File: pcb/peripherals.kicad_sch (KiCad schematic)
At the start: 5 parts, among them J10 SPI, J14 SERIAL, J3 INDICATOR, J8 QWIIC1, J9 QWIIC2

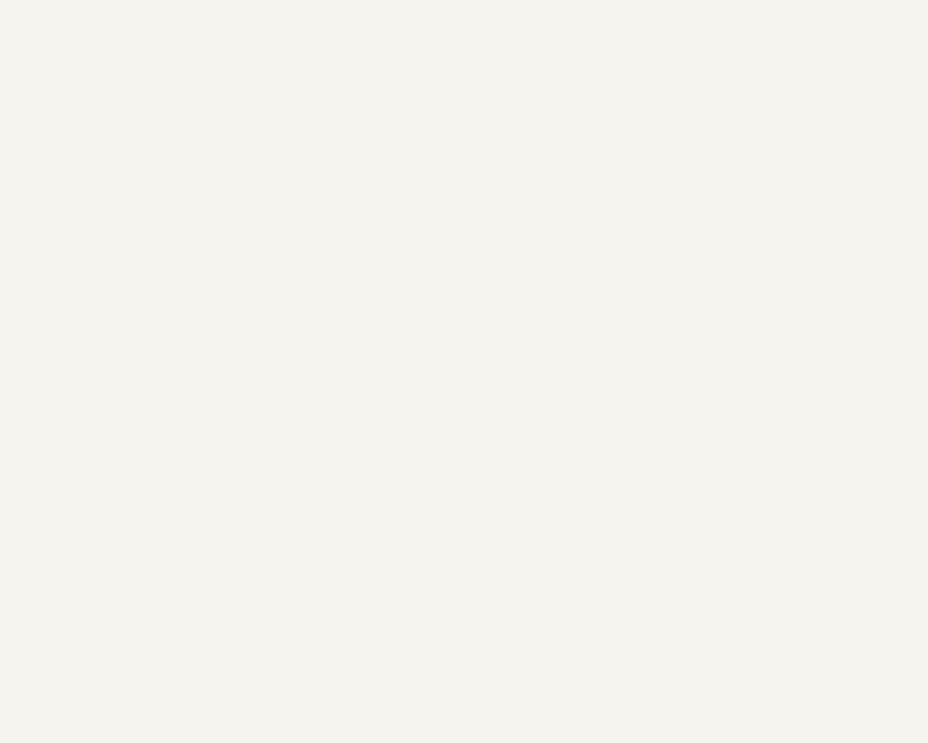
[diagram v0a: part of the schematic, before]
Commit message: Added buzzer
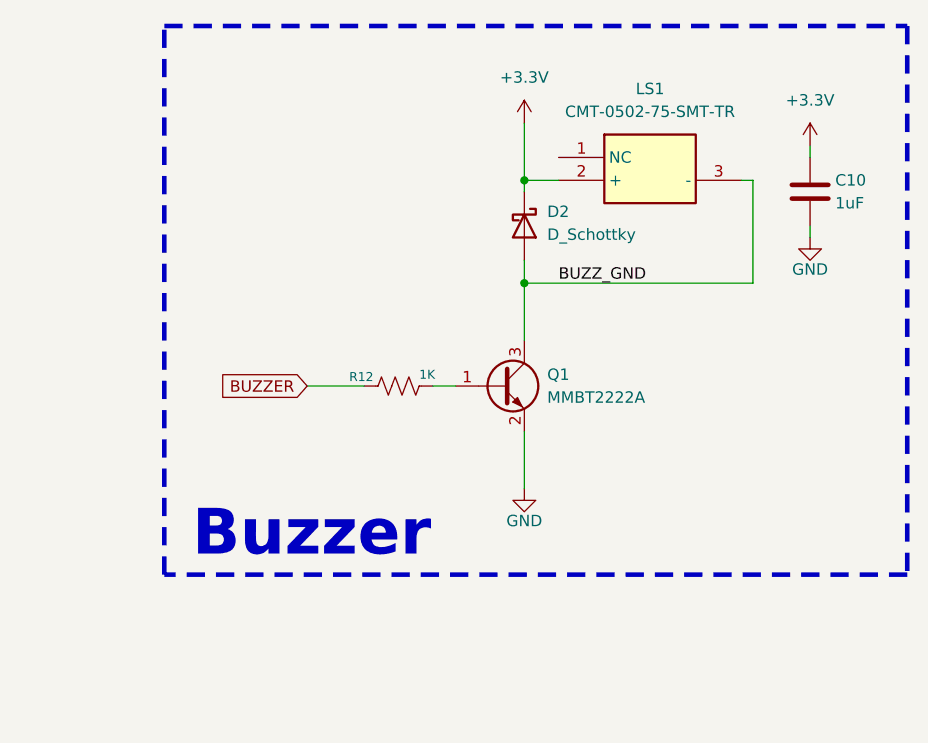
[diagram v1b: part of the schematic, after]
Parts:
- added C10: 1uF, Capacitor_SMD:C_0603_1608Metric, symbol Device:C
- added D2: D_Schottky, Diode_SMD:D_SOD-523, symbol Device:D_Schottky
- added LS1: CMT-0502-75-SMT-TR, CRG Makes:CMT050275SMTTR, symbol CRG Makes:CMT-0502-75-SMT-TR
- added Q1: MMBT2222A, Package_TO_SOT_SMD:SOT-523, symbol Transistor_BJT:MMBT2222A
- added R12: 1K, Resistor_SMD:R_0603_1608Metric, symbol Device:R_US
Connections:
- net +3.3V: now also C10.1, D2.1 (K), LS1.2 (+)
- net GND: now also C10.2, Q1.2 (E)
- new net: Q1.1 (B), R12.2
- new net BUZZER: R12.1
- new net BUZZ_GND: D2.2 (A), LS1.3 (-), Q1.3 (C)
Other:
- note added: "Buzzer"

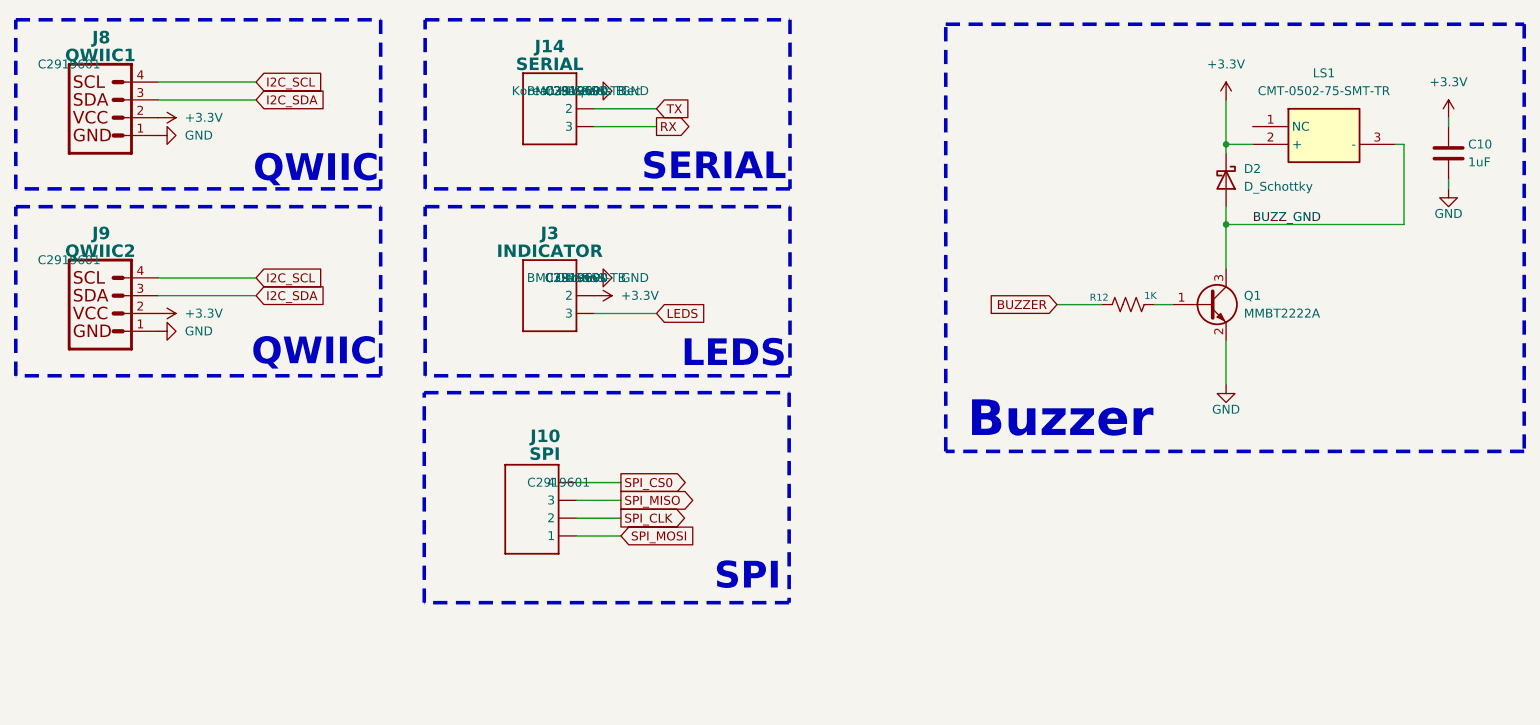
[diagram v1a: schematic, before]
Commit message: Changed SPI to 8 pin connector
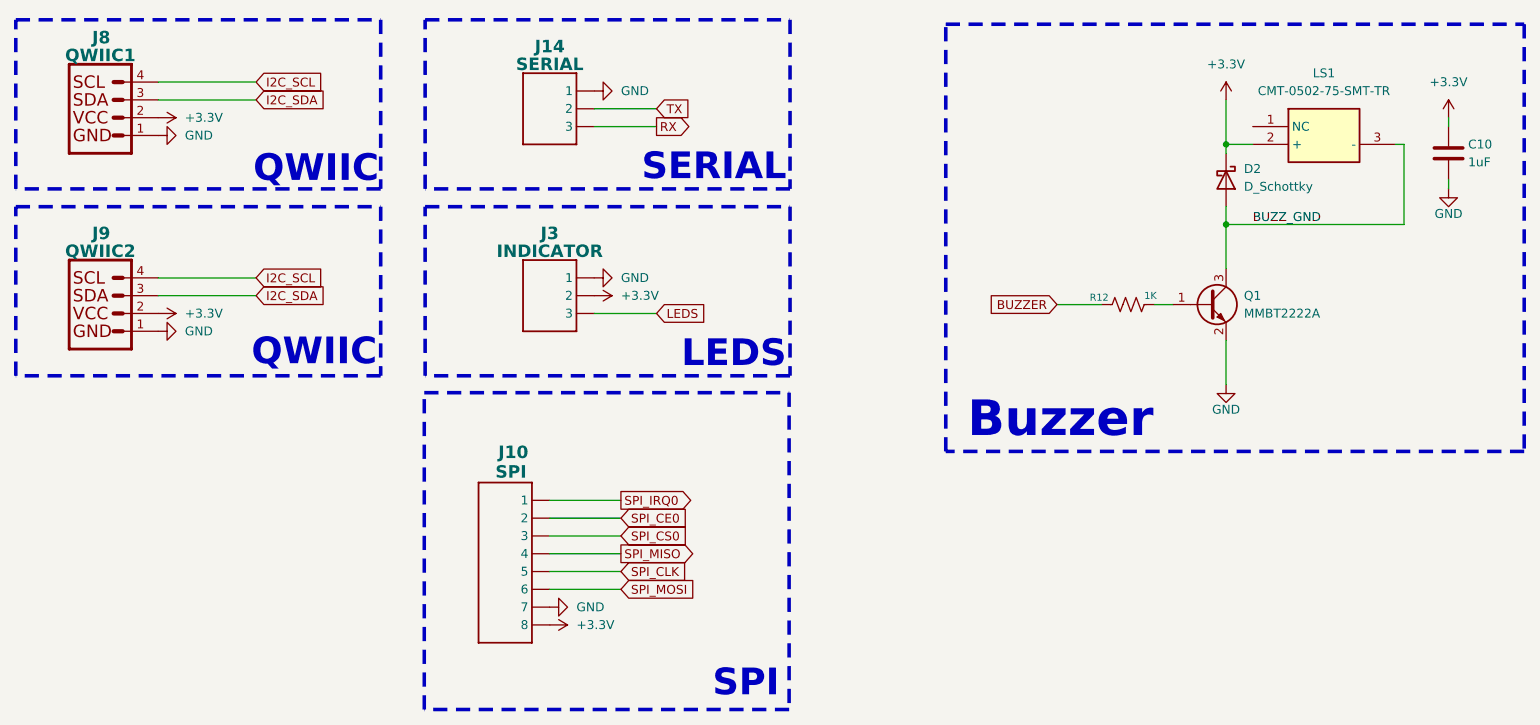
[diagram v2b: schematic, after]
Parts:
- J10: footprint CRGM Connector:JST_SH_BM04B-SRSS-TB_1x04-1MP_P1.00mm_Vertical -> Connector_JST:JST_SH_BM08B-SRSS-TB_1x08-1MP_P1.00mm_Vertical; symbol CRGM Connector:JST-SH-4 -> CRGM Connector:JST-SH-8
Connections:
- net +3.3V: now also J10.8
- net GND: now also J10.7
- net SPI_CLK: now also J10.5; no longer J10.2
- net SPI_CS0: now also J10.3; no longer J10.4
- net SPI_MISO: now also J10.4; no longer J10.3
- net SPI_MOSI: now also J10.6; no longer J10.1
- new net SPI_CE0: J10.2
- new net SPI_IRQ0: J10.1

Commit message: Added additional labels; minor clean up.
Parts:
- J10: Digikey (none) -> 455-BM08B-SRSS-TBTR-ND; LCSC C2919601 -> C2845376; MPN BM04B-SRSS-TB -> BM08B-SRSS-TB(LF)(SN); Mouser (none) -> 306-BM08BSRSSTBLFSN
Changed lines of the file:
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@@
 			)
 		)
-		(property "Description" "JST SH 1.0mm 6 Position"
+		(property "Description" "8 position, 1mm connector"
 			(at 107.95 81.28 0)
 			(effects
@@
 			)
 		)
-		(property "MPN" "BM04B-SRSS-TB"
+		(property "MPN" "BM08B-SRSS-TB(LF)(SN)"
 			(at 107.95 81.28 0)
 			(effects
@@
 			)
 		)
-		(property "LCSC" "C2919601"
+		(property "LCSC" "C2845376"
 			(at 107.95 81.28 0)
 			(effects
@@
 			)
 		)
-		(property "Mouser" ""
+		(property "Mouser" "306-BM08BSRSSTBLFSN"
 			(at 107.95 81.28 0)
 			(effects
@@
 			)
 		)
-		(property "Digikey" ""
+		(property "Digikey" "455-BM08B-SRSS-TBTR-ND"
 			(at 107.95 81.28 0)
 			(effects

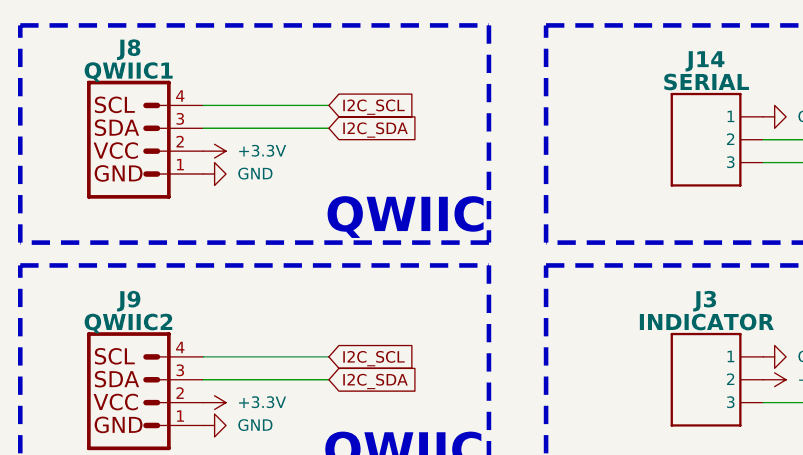
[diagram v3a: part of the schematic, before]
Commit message: Change panel to be 1x1
Changed connectors be vertical rather than horizontal.
Updated TVS diodes to DFN1006 rather than SMF
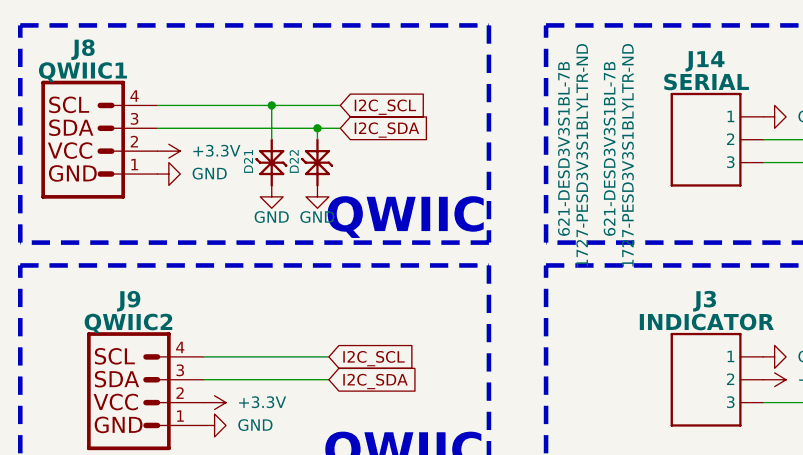
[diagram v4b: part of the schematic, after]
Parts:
- added D21, D22: PESD3V3S1BL, CRGM Passive:DFN1006-2, symbol CRGM Passive:PESD3V3S1BL
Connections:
- net GND: now also D21.1 (K1), D22.1 (K1)
- net I2C_SCL: now also D21.2 (K2)
- net I2C_SDA: now also D22.2 (K2)
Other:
- moved on the sheet: J8

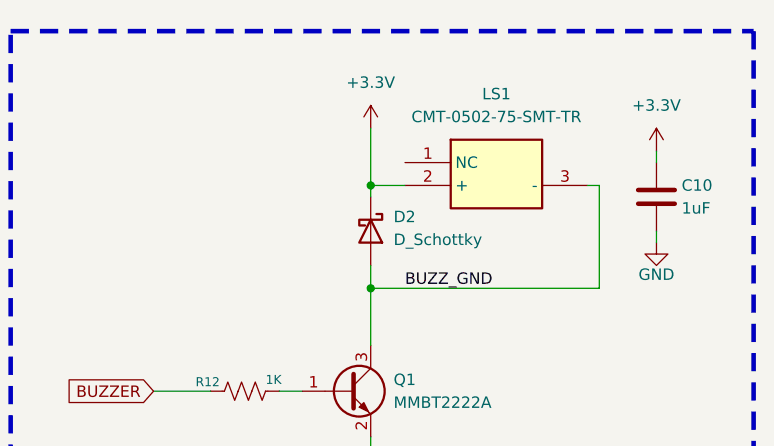
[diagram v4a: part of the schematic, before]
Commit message: Major overhaul of IO
Added GPIO module
Added SPI interface
Added serial interface
Added power selection
Added power LEDs
Changed v3.3 LDO
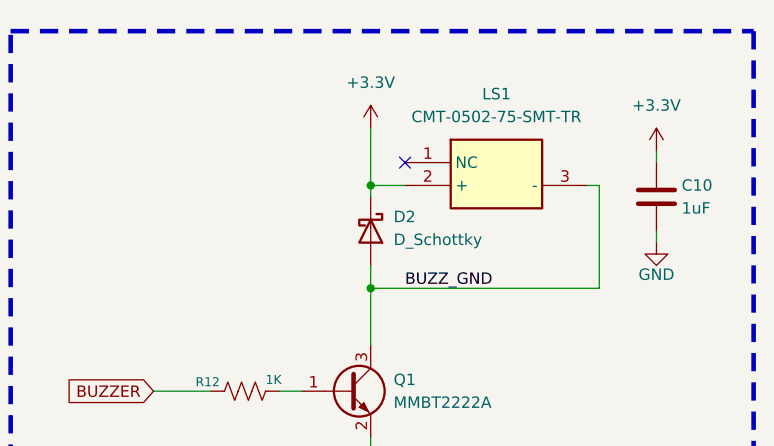
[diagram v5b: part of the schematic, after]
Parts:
- J10: footprint Connector_JST:JST_SH_BM08B-SRSS-TB_1x08-1MP_P1.00mm_Vertical -> CRGM Connector:JST_SH_BM08B-SRSS-TB_1x08-1MP_P1.00mm_Vertical
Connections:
- no-connect marks 0 -> 1

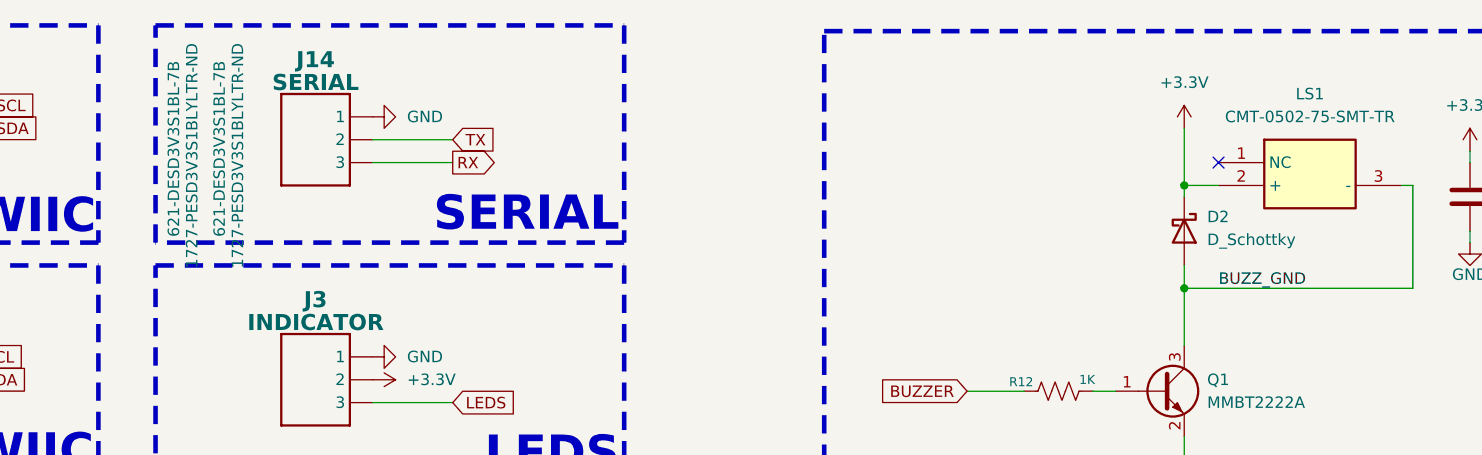
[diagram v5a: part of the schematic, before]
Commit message: Fixed MPN mismatches and other fields
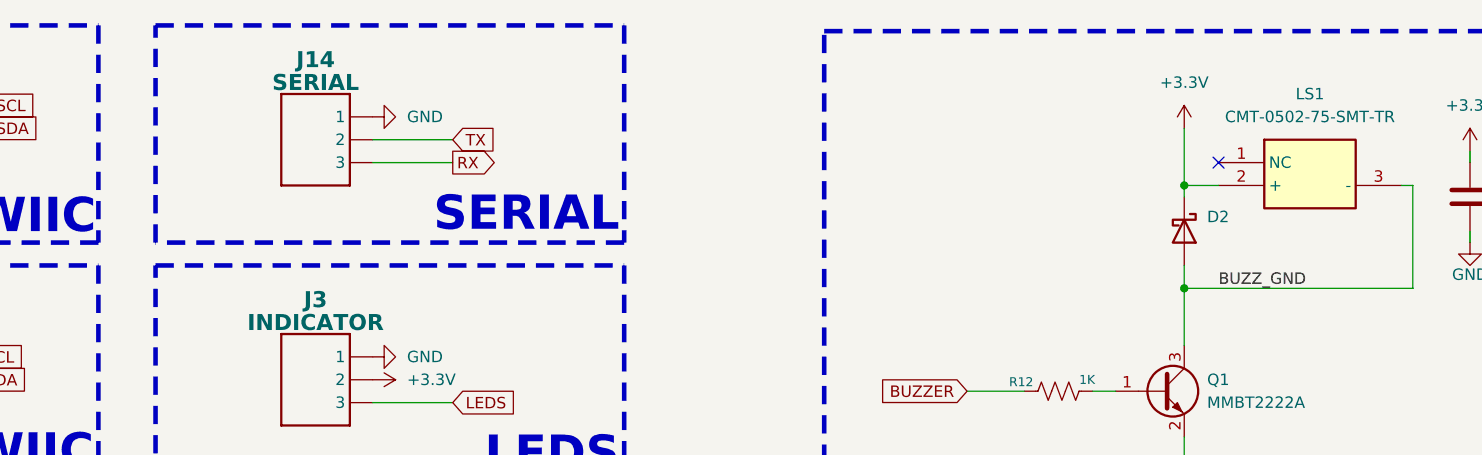
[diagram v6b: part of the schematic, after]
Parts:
- J14: footprint CRGM Connector:JST_SH_BM03B-SRSS-TB_1x03-1MP_P1.00mm_Vertical -> Connector_JST:JST_SH_BM03B-SRSS-TB_1x03-1MP_P1.00mm_Vertical; MN Korean Hroparts Elec -> JST
- J3: MN Omron -> JST
- LS1: MF (none) -> Same Sky
- Q1: MF (none) -> Diodes Incorporated
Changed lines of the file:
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@@
 					(size 1.27 1.27)
 				)
+				(hide yes)
 			)
 		)
@@
 					(size 1.27 1.27)
 				)
+				(hide yes)
 			)
 		)
@@
 					(size 1.27 1.27)
 				)
+				(hide yes)
 			)
 		)
@@
 					(size 1.27 1.27)
 				)
+				(hide yes)
+			)
+		)
+		(property "Digikey" ""
+			(at 193.04 55.88 0)
+			(effects
+				(font
+					(size 1.27 1.27)
+				)
+				(hide yes)
+			)
+		)
+		(property "Mouser" ""
+			(at 193.04 55.88 0)
+			(effects
+				(font
+					(size 1.27 1.27)
+				)
+				(hide yes)
 			)
 		)
@@
 				)
 				(justify left)
+				(hide yes)
 			)
 		)
@@
 					(size 1.27 1.27)
 				)
+				(hide yes)
 			)
 		)
@@
 					(size 1.27 1.27)
 				)
+				(hide yes)
 			)
 		)
@@
 					(size 1.27 1.27)
 				)
+				(hide yes)
 			)
 		)
@@
 					(size 1.27 1.27)
 				)
+				(hide yes)
+			)
+		)
+		(property "Digikey" ""
+			(at 207.01 38.1 0)
+			(effects
+				(font
+					(size 1.27 1.27)
+				)
+				(hide yes)
+			)
+		)
+		(property "Mouser" ""
+			(at 207.01 38.1 0)
+			(effects
+				(font
+					(size 1.27 1.27)
+				)
+				(hide yes)
 			)
 		)
@@
 					(size 1.27 1.27)
 				)
+				(hide yes)
 			)
 		)
@@
 					(size 1.27 1.27)
 				)
+				(hide yes)
 			)
 		)
@@
 					(size 1.27 1.27)
 				)
+				(hide yes)
 			)
 		)
@@
 					(size 1.27 1.27)
 				)
+				(hide yes)
 			)
 		)
@@
 					(size 1.27 1.27)
 				)
+				(hide yes)
 			)
 		)
@@
 					(size 1.27 1.27)
 				)
+				(hide yes)
 			)
 		)
@@
 					(size 1.27 1.27)
 				)
+				(hide yes)
 			)
 		)
@@
 					(size 1.27 1.27)
 				)
+				(hide yes)
 			)
 		)
@@
 					(size 1.27 1.27)
 				)
+				(hide yes)
 			)
 		)
@@
 					(size 1.27 1.27)
 				)
+				(hide yes)
+			)
+		)
+		(property "MF" "Diodes Incorporated"
+			(at 204.47 55.88 0)
+			(effects
+				(font
+					(size 1.27 1.27)
+				)
+				(hide yes)
 			)
 		)
@@
 					(size 1.27 1.27)
 				)
+				(hide yes)
 			)
 		)
@@
 					(size 1.27 1.27)
 				)
+				(hide yes)
 			)
 		)
@@
 					(size 1.27 1.27)
 				)
+				(hide yes)
 			)
 		)
@@
 					(size 1.27 1.27)
 				)
+				(hide yes)
 			)
 		)
@@
 			)
 		)
-		(property "Footprint" "CRGM Connector:JST_SH_BM03B-SRSS-TB_1x03-1MP_P1.00mm_Vertical"
+		(property "Footprint" "Connector_JST:JST_SH_BM03B-SRSS-TB_1x03-1MP_P1.00mm_Vertical"
 			(at 113.03 16.51 0)
 			(effects
@@
 			)
 		)
-		(property "MN" "Korean Hroparts Elec"
+		(property "MN" "JST"
 			(at 114.3 25.4 0)
 			(effects
@@
 					(size 1.27 1.27)
 				)
+				(hide yes)
 			)
 		)
@@
 					(size 1.27 1.27)
 				)
+				(hide yes)
 			)
 		)
@@
 					(size 1.27 1.27)
 				)
+				(hide yes)
 			)
 		)
@@
 					(size 1.27 1.27)
 				)
+				(hide yes)
+			)
+		)
+		(property "Digikey" ""
+			(at 114.3 25.4 0)
+			(effects
+				(font
+					(size 1.27 1.27)
+				)
+				(hide yes)
+			)
+		)
+		(property "Mouser" ""
+			(at 114.3 25.4 0)
+			(effects
+				(font
+					(size 1.27 1.27)
+				)
+				(hide yes)
 			)
 		)
@@
 					(size 1.27 1.27)
 				)
+				(hide yes)
 			)
 		)
@@
 					(size 1.27 1.27)
 				)
+				(hide yes)
 			)
 		)
@@
 					(size 1.27 1.27)
 				)
+				(hide yes)
 			)
 		)
@@
 					(size 1.27 1.27)
 				)
+				(hide yes)
+			)
+		)
+		(property "Digikey" ""
+			(at 238.76 34.29 0)
+			(effects
+				(font
+					(size 1.27 1.27)
+				)
+				(hide yes)
+			)
+		)
+		(property "Mouser" ""
+			(at 238.76 34.29 0)
+			(effects
+				(font
+					(size 1.27 1.27)
+				)
+				(hide yes)
 			)
 		)
@@
 					(size 1.27 1.27)
 				)
+				(hide yes)
 			)
 		)
@@
 					(size 1.27 1.27)
 				)
+				(hide yes)
 			)
 		)
@@
 					(size 1.27 1.27)
 				)
+				(hide yes)
 			)
 		)
@@
 					(size 1.27 1.27)
 				)
+				(hide yes)
 			)
 		)
@@
 					(size 1.27 1.27)
 				)
+				(hide yes)
 			)
 		)
@@
 					(size 1.27 1.27)
 				)
+				(hide yes)
 			)
 		)
@@
 					(size 1.27 1.27)
 				)
+				(hide yes)
 			)
 		)
@@
 					(size 1.27 1.27)
 				)
+				(hide yes)
 			)
 		)
@@
 					(size 1.27 1.27)
 				)
+				(hide yes)
 			)
 		)
@@
 					(size 1.27 1.27)
 				)
+				(hide yes)
 			)
 		)
@@
 					(size 1.27 1.27)
 				)
+				(hide yes)
 			)
 		)
@@
 					(size 1.27 1.27)
 				)
+				(hide yes)
 			)
 		)
@@
 					(size 1.27 1.27)
 				)
+				(hide yes)
 			)
 		)
@@
 					(size 1.27 1.27)
 				)
+				(hide yes)
 			)
 		)
@@
 					(size 1.27 1.27)
 				)
+				(hide yes)
 			)
 		)
@@
 					(size 1.27 1.27)
 				)
+				(hide yes)
 			)
 		)
@@
 					(size 1.27 1.27)
 				)
+				(hide yes)
+			)
+		)
+		(property "MF" "Same Sky"
+			(at 210.82 30.48 0)
+			(effects
+				(font
+					(size 1.27 1.27)
+				)
+				(hide yes)
+			)
+		)
+		(property "Digikey" ""
+			(at 210.82 30.48 0)
+			(effects
+				(font
+					(size 1.27 1.27)
+				)
+				(hide yes)
 			)
 		)
@@
 			)
 		)
-		(property "MN" "Omron"
+		(property "MN" "JST"
 			(at 114.3 52.07 0)
 			(effects
@@
 					(size 1.27 1.27)
 				)
+				(hide yes)
 			)
 		)
@@
 					(size 1.27 1.27)
 				)
+				(hide yes)
 			)
 		)
@@
 					(size 1.27 1.27)
 				)
+				(hide yes)
 			)
 		)
@@
 					(size 1.27 1.27)
 				)
-			)
-		)
+				(hide yes)
+			)
+		)
+		(property "Digikey" ""
+			(at 114.3 52.07 0)
+			(effects
+				(font
+					(size 1.27 1.27)
+				)
+				(hide yes)
+			)
+		)
+		(property "Mouser" ""
+			(at 114.3 52.07 0)
+			(effects
+				(font
+					(size 1.27 1.27)
+				)
+				(hide yes)
+			)
+		)
